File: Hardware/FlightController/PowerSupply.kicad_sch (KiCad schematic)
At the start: 12 parts, among them J1 Conn_01x02, U3 LMR54410DBVR

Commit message: Add ICM-42670-P symbol and schematic
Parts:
- added F1: 750mA, symbol Device:Fuse_Small
- R7: value 1.5k -> 1k
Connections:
- net +3V3: now also F1.2; no longer C4.1, C5.1, L1.2, R1.1
- new net: C4.1, C5.1, F1.1, L1.2, R1.1
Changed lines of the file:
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@@
+    (stroke (width 0) (type default) (color 0 0 0 0))
+  )
+  (wire (pts (xy 212.09 90.17) (xy 215.9 90.17))
     (stroke (width 0) (type default) (color 0 0 0 0))
   )
@@
     (stroke (width 0) (type default) (color 0 0 0 0))
   )
-  (wire (pts (xy 212.09 90.17) (xy 218.44 90.17))
-    (stroke (width 0) (type default) (color 0 0 0 0))
-  )
   (wire (pts (xy 119.38 87.63) (xy 119.38 85.09))
     (stroke (width 0) (type default) (color 0 0 0 0))
@@
     (stroke (width 0) (type default) (color 0 0 0 0))
   )
+  (wire (pts (xy 220.98 90.17) (xy 224.79 90.17))
+    (stroke (width 0) (type default) (color 0 0 0 0))
+  )
   (symbol (lib_id "power:+BATT") (at 68.58 96.52 270) (unit 1)
     (in_bom yes) (on_board yes) (fields_autoplaced)
@@
     (pin "1")
   )
-  (symbol (lib_id "power:+3.3V") (at 218.44 90.17 0) (unit 1)
-    (in_bom yes) (on_board yes) (fields_autoplaced)
-    (property "Reference" "#PWR03" (id 0) (at 218.44 93.98 0)
-      (effects (font (size 1.27 1.27)) hide)
-    )
-    (property "Value" "+3.3V" (id 1) (at 218.44 85.09 0))
-    (property "Footprint" "" (id 2) (at 218.44 90.17 0)
-      (effects (font (size 1.27 1.27)) hide)
-    )
-    (property "Datasheet" "" (id 3) (at 218.44 90.17 0)
+  (symbol (lib_id "power:+3.3V") (at 224.79 90.17 0) (unit 1)
+    (in_bom yes) (on_board yes) (fields_autoplaced)
+    (property "Reference" "#PWR03" (id 0) (at 224.79 93.98 0)
+      (effects (font (size 1.27 1.27)) hide)
+    )
+    (property "Value" "+3.3V" (id 1) (at 224.79 85.09 0))
+    (property "Footprint" "" (id 2) (at 224.79 90.17 0)
+      (effects (font (size 1.27 1.27)) hide)
+    )
+    (property "Datasheet" "" (id 3) (at 224.79 90.17 0)
       (effects (font (size 1.27 1.27)) hide)
     )
@@
       (effects (font (size 1.27 1.27)) (justify left))
     )
-    (property "Value" "1.5k" (id 1) (at 237.49 104.1399 0)
+    (property "Value" "1k" (id 1) (at 237.49 104.1399 0)
       (effects (font (size 1.27 1.27)) (justify left))
     )
@@
       (effects (font (size 1.27 1.27)) hide)
     )
+    (pin "1")
+    (pin "2")
+  )
+  (symbol (lib_id "Device:Fuse_Small") (at 218.44 90.17 0) (unit 1)
+    (in_bom yes) (on_board yes) (fields_autoplaced)
+    (property "Reference" "F1" (id 0) (at 218.44 85.09 0))
+    (property "Value" "750mA" (id 1) (at 218.44 87.63 0))
+    (property "Footprint" "" (id 2) (at 218.44 90.17 0)
+      (effects (font (size 1.27 1.27)) hide)
+    )
+    (property "Datasheet" "~" (id 3) (at 218.44 90.17 0)
+      (effects (font (size 1.27 1.27)) hide)
+    )

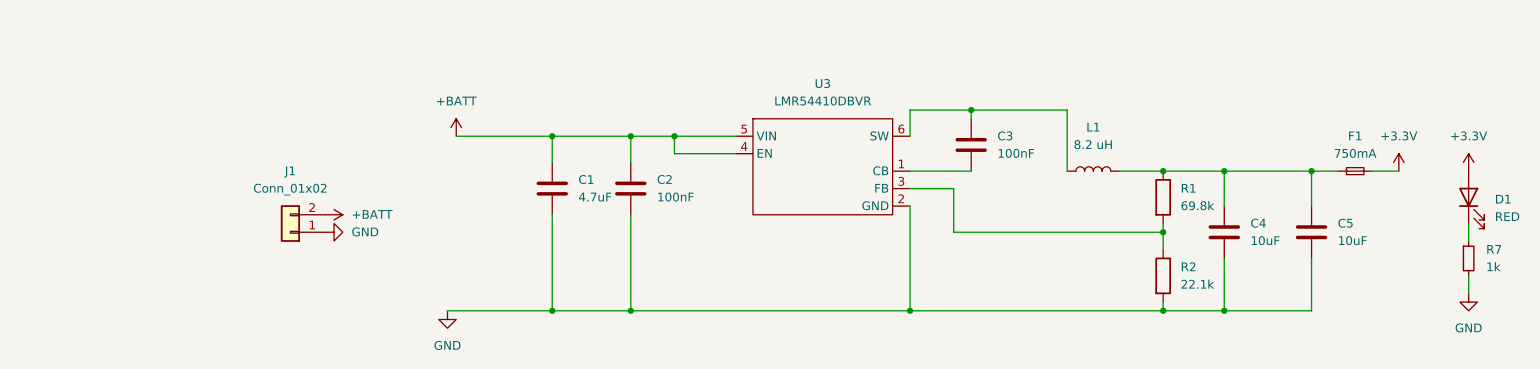
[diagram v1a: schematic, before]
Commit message: Round out basic schematic and add preliminary board layout
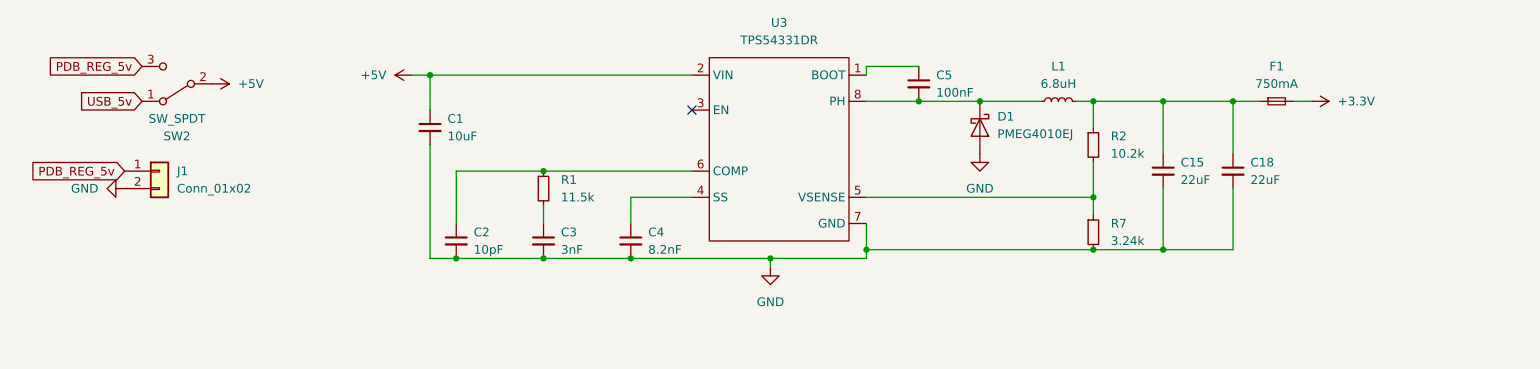
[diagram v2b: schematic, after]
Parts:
- removed C1: 4.7uF, Capacitor_SMD:C_0603_1608Metric, symbol Device:C
- removed C2, C3: 100nF, Capacitor_SMD:C_0603_1608Metric, symbol Device:C
- removed C4, C5: 10uF, Capacitor_SMD:C_0603_1608Metric, symbol Device:C
- removed D1: RED, LED_SMD:LED_0603_1608Metric, symbol Device:LED
- removed L1: 8.2 uH, symbol Device:L
- removed R1: 69.8k, Resistor_SMD:R_0603_1608Metric, symbol Device:R
- removed R2: 22.1k, Resistor_SMD:R_0603_1608Metric, symbol Device:R
- removed U3: LMR54410DBVR, Package_TO_SOT_SMD:SOT-23-6, symbol FlightControllerLibrary:LMR54410DBVR
- added C1: 10uF, Capacitor_SMD:C_0402_1005Metric, symbol Device:C_Small
- added C15, C18: 22uF, Capacitor_SMD:C_0402_1005Metric, symbol Device:C_Small
- added C2: 10pF, Capacitor_SMD:C_0402_1005Metric, symbol Device:C_Small
- added C3: 3nF, Capacitor_SMD:C_0402_1005Metric, symbol Device:C_Small
- added C4: 8.2nF, Capacitor_SMD:C_0402_1005Metric, symbol Device:C_Small
- added C5: 100nF, Capacitor_SMD:C_0402_1005Metric, symbol Device:C_Small
- added D1: PMEG4010EJ, Diode_SMD:D_SOD-323F, symbol Diode:PMEG4010EJ
- added L1: 6.8uH, Inductor_SMD:L_0402_1005Metric, symbol Device:L_Small
- added R1: 11.5k, Resistor_SMD:R_0402_1005Metric, symbol Device:R_Small
- added R2: 10.2k, Resistor_SMD:R_0402_1005Metric, symbol Device:R_Small
- added SW2: SW_SPDT, Button_Switch_THT:SW_Slide_1P2T_CK_OS102011MS2Q, symbol Switch:SW_SPDT
- added U3: TPS54331DR, Package_SO:SOIC-8_3.9x4.9mm_P1.27mm, symbol FlightControllerLibrary:TPS54331DR
- F1: footprint (none) -> Fuse:Fuse_0402_1005Metric
- J1: footprint (none) -> Connector_PinSocket_2.54mm:PinSocket_1x02_P2.54mm_Horizontal
- R7: value 1k -> 3.24k; footprint Resistor_SMD:R_0603_1608Metric -> Resistor_SMD:R_0402_1005Metric
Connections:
- net +BATT is gone; now on net GND: J1.2 (Pin_2)
- net GND: now also C1.2, C15.2, C18.2, C2.2, C3.2, C4.2, D1.2 (A), U3.7 (GND); no longer J1.1 (Pin_1)
- net at F1.1: now also C15.1, C18.1, L1.2, R2.1
- net at R7.1: now also R2.2, U3.5 (VSENSE)
- new net: C5.1, U3.1 (BOOT)
- new net: C5.2, D1.1 (K), L1.1, U3.8 (PH)
- new net: C3.1, R1.2
- new net: C4.1, U3.4 (SS)
- new net: C2.1, R1.1, U3.6 (COMP)
- new net +5V: C1.1, SW2.2 (B), U3.2 (VIN)
- new net PDB_REG_5v: J1.1 (Pin_1), SW2.3 (C)
- new net USB_5v: SW2.1 (A)
- no-connect marks 0 -> 1

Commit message: Update footprints to be digikey compliant
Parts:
- J1: footprint Connector_PinSocket_2.54mm:PinSocket_1x02_P2.54mm_Horizontal -> Connector_PinHeader_2.54mm:PinHeader_1x02_P2.54mm_Vertical
- SW2: footprint Button_Switch_THT:SW_Slide_1P2T_CK_OS102011MS2Q -> digikey-footprints:Switch_Slide_11.6x4mm_EG1218
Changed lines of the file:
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@@
       (effects (font (size 1.27 1.27)) (justify left))
     )
-    (property "Footprint" "Connector_PinSocket_2.54mm:PinSocket_1x02_P2.54mm_Horizontal" (id 2) (at 44.45 90.17 0)
+    (property "Footprint" "Connector_PinHeader_2.54mm:PinHeader_1x02_P2.54mm_Vertical" (id 2) (at 44.45 90.17 0)
       (effects (font (size 1.27 1.27)) hide)
     )
@@
     (property "Reference" "SW2" (id 0) (at 46.99 85.09 0))
     (property "Value" "SW_SPDT" (id 1) (at 46.99 82.55 0))
-    (property "Footprint" "Button_Switch_THT:SW_Slide_1P2T_CK_OS102011MS2Q" (id 2) (at 46.99 77.47 0)
-      (effects (font (size 1.27 1.27)) hide)
-    )
+    (property "Footprint" "digikey-footprints:Switch_Slide_11.6x4mm_EG1218" (id 2) (at 46.99 77.47 0)
+      (effects (font (size 1.27 1.27)) hide)
+    )

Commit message: Update footprints, routing and LCSC numbers
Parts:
- removed C18: 22uF, Capacitor_SMD:C_0402_1005Metric, symbol Device:C_Small
- removed F1: 750mA, Fuse:Fuse_0402_1005Metric, symbol Device:Fuse_Small
- added D2: LED, LED_SMD:LED_0603_1608Metric, symbol Device:LED
- added R12: 10k, Resistor_SMD:R_0603_1608Metric, symbol Device:R_Small
- C15: renamed from C1; footprint Capacitor_SMD:C_0402_1005Metric -> Capacitor_SMD:C_0603_1608Metric; LCSC (none) -> C9446
- C16: renamed from C2; footprint Capacitor_SMD:C_0402_1005Metric -> Capacitor_SMD:C_0603_1608Metric; LCSC (none) -> C1634
- C17: renamed from C3; value 3nF -> 1nF; footprint Capacitor_SMD:C_0402_1005Metric -> Capacitor_SMD:C_0603_1608Metric; LCSC (none) -> C1588
- C18: renamed from C4; footprint Capacitor_SMD:C_0402_1005Metric -> Capacitor_SMD:C_0603_1608Metric; LCSC (none) -> C27920
- C19: renamed from C5; footprint Capacitor_SMD:C_0402_1005Metric -> Capacitor_SMD:C_0603_1608Metric; LCSC (none) -> C14663
- C20: renamed from C15; value 22uF -> 100uF; footprint Capacitor_SMD:C_0402_1005Metric -> Capacitor_SMD:C_1206_3216Metric; LCSC (none) -> C15008
- D1: value PMEG4010EJ -> SS14; footprint Diode_SMD:D_SOD-323F -> Diode_SMD:D_SMA; LCSC (none) -> C2480
- L1: value 6.8uH -> 3.3uH; footprint Inductor_SMD:L_0402_1005Metric -> Inductor_SMD:L_1008_2520Metric_Pad1.43x2.20mm_HandSolder; dk (none) -> y
- R10: renamed from R2; footprint Resistor_SMD:R_0402_1005Metric -> Resistor_SMD:R_0805_2012Metric_Pad1.20x1.40mm_HandSolder; dk (none) -> y
- R11: renamed from R7; footprint Resistor_SMD:R_0402_1005Metric -> Resistor_SMD:R_0603_1608Metric_Pad0.98x0.95mm_HandSolder; dk (none) -> y
- R9: renamed from R1; value 11.5k -> 41.2k; footprint Resistor_SMD:R_0402_1005Metric -> Resistor_SMD:R_0603_1608Metric_Pad0.98x0.95mm_HandSolder; dk (none) -> y
- SW2: dk (none) -> y
- U5: renamed from U3; LCSC (none) -> C9865
- renumbered J1 to J13
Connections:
- net +3V3: now also C20.1, L1.2, R10.1, D2.2 (A)
- net GND: now also R12.2
- new net: D2.1 (K), R12.1

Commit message: Finalize design and routing for v1.0 fab
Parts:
- C15: LCSC C9446 -> C96446
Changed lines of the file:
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@@
       (effects (font (size 1.27 1.27)) hide)
     )
-    (property "LCSC" "C9446" (id 4) (at 83.82 83.82 0)
+    (property "LCSC" "C96446" (id 4) (at 83.82 83.82 0)
       (effects (font (size 1.27 1.27)) hide)
     )
